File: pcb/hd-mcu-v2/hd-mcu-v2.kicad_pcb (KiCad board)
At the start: 2 copper layers, 70 x 48 mm, 27 parts

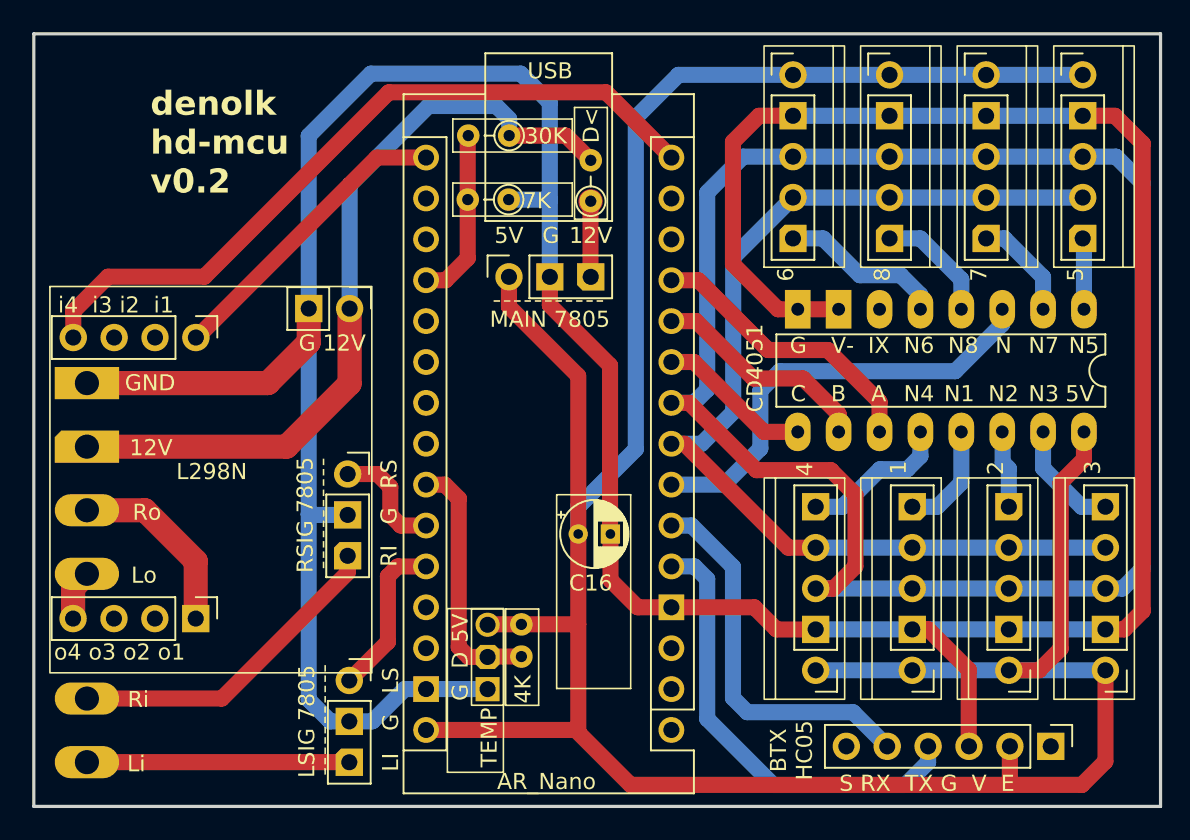
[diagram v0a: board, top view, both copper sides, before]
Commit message: refactor Ax sensor pin layout
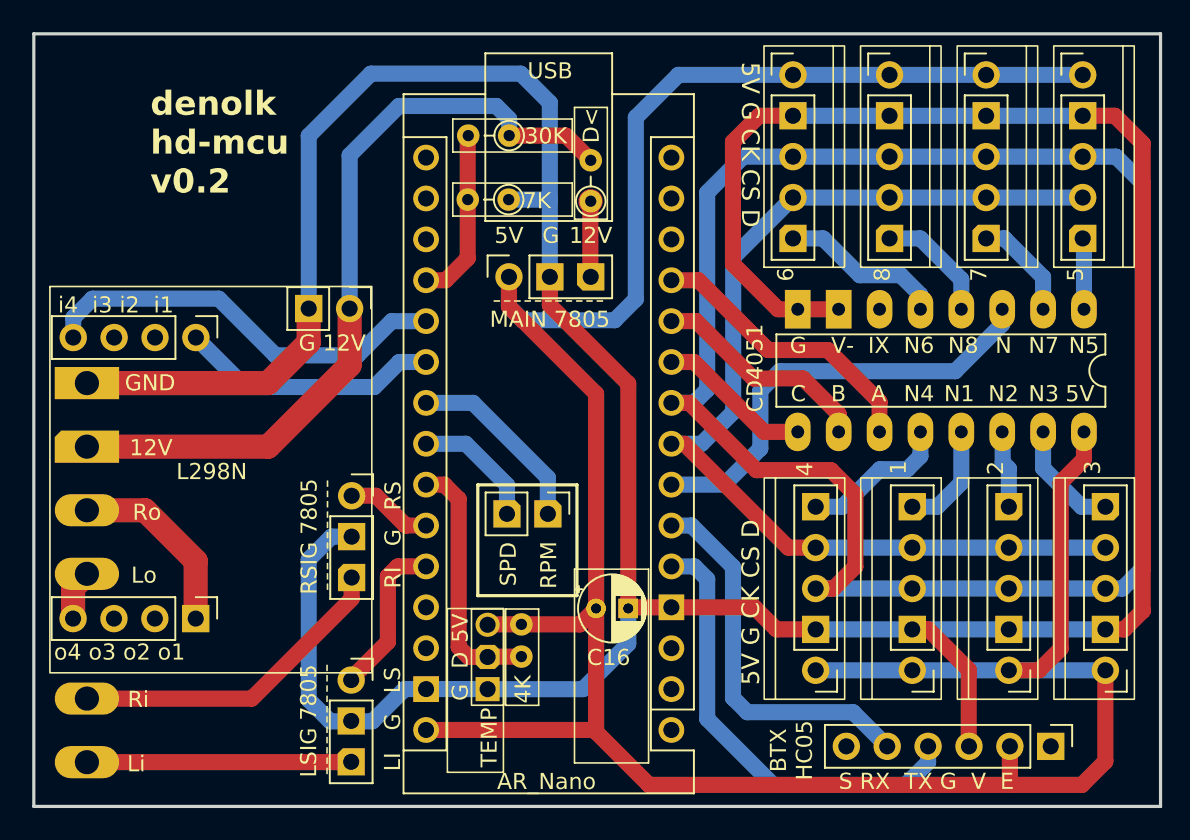
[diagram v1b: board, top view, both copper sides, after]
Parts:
- added REF**: C16, Capacitor_THT:CP_Radial_D4.0mm_P2.00mm, F.Cu at (59.6, 71.3)
- added REF**: PinHeader_1x02_P2.54mm_Vertical, Connector_PinHeader_2.54mm:PinHeader_1x02_P2.54mm_Vertical, F.Cu at (56.6, 65.5)
- REF**: moved to B.Cu
- moved REF** 4.76 mm to (59.6, 71.3)
- moved RSIG 7805 1.37 mm to (44.4, 64.3)
- moved LSIG 7805 0.12 mm to (44.3, 75.8)
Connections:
- REF** pad A1: D15 -> D_SIG_L_OUT
- REF** pad A2: D16 -> D_SIG_R_OUT
- REF** pad A3: D17 -> D_RPM
- REF** pad A4: D18 -> D_SPD
- REF** pad D12: D_SIG_L_OUT -> D12
- REF** pad D13: D_SIG_R_OUT -> D13
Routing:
- net D_SIG_L_OUT: track 46.1 -> 26.0 mm
- net D_RPM: track 0.00 -> 11.7 mm
- net D_SPD: track 0.00 -> 7.88 mm
- net 5V: track 180.1 -> 176.6 mm
- net D_SIG_R_OUT: track 18.9 -> 16.2 mm
- net GND: track 233.7 -> 231.5 mm
- net D_SIG_R_IN: track 7.26 -> 5.42 mm
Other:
- board text added: "5V G CK CS D"
- board text added: "RPM"
- board text added: "S RX TX G V E"
- board text added: "SPD"

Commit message: pcb routing optimize
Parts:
- moved 30K 12.6 mm to (44.2, 49.8), turned to 90 degrees
- moved REF** 11.0 mm to (59.4, 60.3) (x2)
- moved 7K 10.6 mm to (44.2, 42.1), turned to -90 degrees
- moved -> 5.54 mm to (56.6, 41.1), turned to 0 degrees
- moved MAIN 7805 5.09 mm to (54.1, 45.7)
- moved REF** 2.97 mm to (56.0, 62.6)
- renumbered D< to ->
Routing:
- net GND: track 231.5 -> 221.7 mm
- net 12V: track 54.4 -> 49.3 mm
- net D_SPD: track 7.88 -> 5.04 mm
- net D_RPM: track 11.7 -> 9.49 mm
- net D_VOLT: track 10.8 -> 10.2 mm

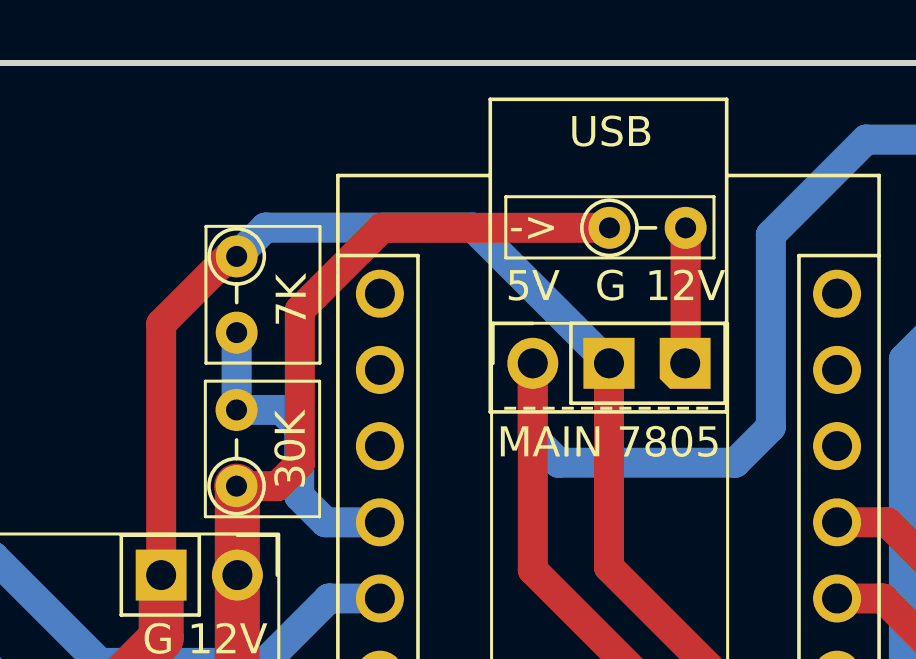
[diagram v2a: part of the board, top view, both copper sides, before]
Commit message: add serial commands
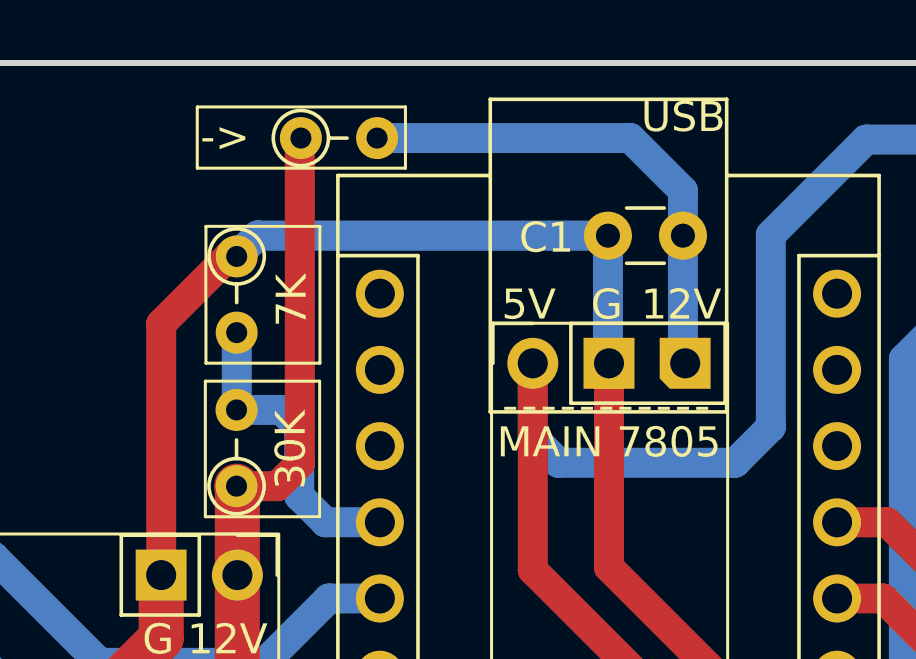
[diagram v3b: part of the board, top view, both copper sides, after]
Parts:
- added REF**: C1, Capacitor_THT:C_Disc_D3.0mm_W1.6mm_P2.50mm, F.Cu at (56.6, 41.4)
- moved -> 10.7 mm to (46.4, 38.1)
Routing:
- net 12V: track 49.3 -> 55.9 mm
- net GND: track 221.7 -> 223.9 mm
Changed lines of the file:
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@@
         (effects (font (size 1 1) (thickness 0.15)))
     )
-    (fp_text user "G" (at 2.570051 2.6 unlocked) (layer "F.SilkS")
-        (effects (font (size 1 1) (thickness 0.15)))
-    )
-    (fp_text user "5V" (at 2.570051 0 unlocked) (layer "F.SilkS")
-        (effects (font (size 1 1) (thickness 0.15)))
-    )
-    (fp_text user "12V" (at 2.570051 5.08 unlocked) (layer "F.SilkS")
+    (fp_text user "G" (at 1.955 2.465 unlocked) (layer "F.SilkS")
+        (effects (font (size 1 1) (thickness 0.15)))
+    )
+    (fp_text user "5V" (at 1.955 -0.135 unlocked) (layer "F.SilkS")
+        (effects (font (size 1 1) (thickness 0.15)))
+    )
+    (fp_text user "12V" (at 1.955 4.945 unlocked) (layer "F.SilkS")
         (effects (font (size 1 1) (thickness 0.15)))
     )
@@
         (effects (font (size 1 1) (thickness 0.15)))
     )
-    (fp_text user "USB" (at 7.5375 40.945 unlocked) (layer "F.SilkS")
+    (fp_text user "USB" (at 5.1275 41.445 unlocked) (layer "F.SilkS")
         (effects (font (size 1 1) (thickness 0.15)))
     )
@@
   )
   (footprint "Resistor_THT:R_Axial_DIN0204_L3.6mm_D1.6mm_P2.54mm_Vertical" (layer "F.Cu")
-    (at 56.65 41.14)
+    (at 46.365 38.1475)
     (descr "Resistor, Axial_DIN0204 series, Axial, Vertical, pin pitch=2.54mm, 0.167W, length*diameter=3.6*1.6mm^2, http://cdn-reichelt.de/documents/datenblatt/B400/1_4W%23YAG.pdf")
     (tags "Resistor Axial_DIN0204 series Axial Vertical pin pitch 2.54mm 0.167W length 3.6mm diameter 1.6mm")
@@
     (pad "3" thru_hole oval (at 0 0 180) (size 4 2) (drill 1.5) (layers "*.Cu" "*.Mask")
       (net 6 "SIG_R_OUT"))
+  )
+  (footprint "Capacitor_THT:C_Disc_D3.0mm_W1.6mm_P2.50mm" (layer "F.Cu")
+    (at 56.6 41.4)
+    (descr "C, Disc series, Radial, pin pitch=2.50mm, , diameter*width=3.0*1.6mm^2, Capacitor, http://www.vishay.com/docs/45233/krseries.pdf")
+    (tags "C Disc series Radial pin pitch 2.50mm  diameter 3.0mm width 1.6mm Capacitor")
+    (attr through_hole)
+    (fp_text reference "REF**" (at 1.25 -2.05) (layer "F.SilkS") hide
+        (effects (font (size 1 1) (thickness 0.15)))
+    )
+    (fp_text value "C1" (at -2.05 0.07) (layer "F.SilkS")
+        (effects (font (size 1 1) (thickness 0.15)))
+    )
+    (fp_text user "${REFERENCE}" (at 1.25 0) (layer "F.Fab") hide
+        (effects (font (size 0.6 0.6) (thickness 0.09)))
+    )
+    (fp_line (start 0.621 -0.92) (end 1.879 -0.92)
+      (stroke (width 0.12) (type solid)) (layer "F.SilkS"))
+    (fp_line (start 0.621 0.92) (end 1.879 0.92)
+      (stroke (width 0.12) (type solid)) (layer "F.SilkS"))
+    (fp_line (start -1.05 -1.05) (end -1.05 1.05)
+      (stroke (width 0.05) (type solid)) (layer "F.CrtYd"))
+    (fp_line (start -1.05 1.05) (end 3.55 1.05)
+      (stroke (width 0.05) (type solid)) (layer "F.CrtYd"))
+    (fp_line (start 3.55 -1.05) (end -1.05 -1.05)
+      (stroke (width 0.05) (type solid)) (layer "F.CrtYd"))
+    (fp_line (start 3.55 1.05) (end 3.55 -1.05)
+      (stroke (width 0.05) (type solid)) (layer "F.CrtYd"))
+    (fp_line (start -0.25 -0.8) (end -0.25 0.8)
+      (stroke (width 0.1) (type solid)) (layer "F.Fab"))
+    (fp_line (start -0.25 0.8) (end 2.75 0.8)
+      (stroke (width 0.1) (type solid)) (layer "F.Fab"))
+    (fp_line (start 2.75 -0.8) (end -0.25 -0.8)
+      (stroke (width 0.1) (type solid)) (layer "F.Fab"))
+    (fp_line (start 2.75 0.8) (end 2.75 -0.8)
+      (stroke (width 0.1) (type solid)) (layer "F.Fab"))
+    (pad "1" thru_hole circle (at 0 0) (size 1.6 1.6) (drill 0.8) (layers "*.Cu" "*.Mask")
+      (net 1 "GND"))
+    (pad "2" thru_hole circle (at 2.5 0) (size 1.6 1.6) (drill 0.8) (layers "*.Cu" "*.Mask")
+      (net 2 "12V"))
+    (model "${KICAD6_3DMODEL_DIR}/Capacitor_THT.3dshapes/C_Disc_D3.0mm_W1.6mm_P2.50mm.wrl"
+      (offset (xyz 0 0 0))
+      (scale (xyz 1 1 1))
+      (rotate (xyz 0 0 0))
+    )
   )
   (footprint "Connector_PinHeader_2.54mm:Socker_PinHeader_1x05_P2.54mm_Dualside" (layer "F.Cu")
@@
   (gr_rect (start 58.099604 57.9) (end 62.699604 69.94)
     (stroke (width 0.1) (type default)) (fill none) (layer "B.SilkS"))
-  (gr_rect (start 60.135 40.1025) (end 53.195 42.1425)
+  (gr_rect (start 49.85 37.11) (end 42.91 39.15)
     (stroke (width 0.1) (type default)) (fill none) (layer "F.SilkS"))
   (gr_rect (start 50.3225 71.355) (end 53.8025 81.525)
@@
   (segment (start 69.395 71.275) (end 64.2375 71.275) (width 1) (layer "F.Cu") (net 1))
   (segment (start 41.7075 54.815) (end 41.7075 52.715) (width 1.5) (layer "F.Cu") (net 1))
+  (segment (start 44.9375 41.4) (end 56.6 41.4) (width 1) (layer "B.Cu") (net 1))
   (segment (start 44.375 66.885) (end 43.125 66.885) (width 1) (layer "B.Cu") (net 1))
   (segment (start 43.0425 78.36) (end 45.6625 78.36) (width 1) (layer "B.Cu") (net 1))
   (segment (start 57.99 76.36) (end 63.075 71.275) (width 1) (layer "B.Cu") (net 1))
   (segment (start 63.075 71.275) (end 64.2375 71.275) (width 1) (layer "B.Cu") (net 1))
-  (segment (start 56.635 45.655) (end 52.11 41.13) (width 1) (layer "B.Cu") (net 1))
   (segment (start 41.7075 77.025) (end 43.0425 78.36) (width 1) (layer "B.Cu") (net 1))
   (segment (start 41.7075 68.3025) (end 41.7075 77.025) (width 1) (layer "B.Cu") (net 1))
   (segment (start 45.6625 78.36) (end 47.6675 76.355) (width 1) (layer "B.Cu") (net 1))
-  (segment (start 52.11 41.13) (end 45.1875 41.13) (width 1) (layer "B.Cu") (net 1))
   (segment (start 52.82 76.36) (end 57.99 76.36) (width 1) (layer "B.Cu") (net 1))
   (segment (start 47.6675 76.355) (end 48.9975 76.355) (width 1) (layer "B.Cu") (net 1))
   (segment (start 73.2025 72.6475) (end 91.2025 72.6475) (width 1) (layer "B.Cu") (net 1))
-  (segment (start 45.1875 41.13) (end 44.225 42.0925) (width 1) (layer "B.Cu") (net 1))
   (segment (start 43.125 66.885) (end 41.7075 68.3025) (width 1) (layer "B.Cu") (net 1))
+  (segment (start 44.9275 41.39) (end 44.9375 41.4) (width 1) (layer "B.Cu") (net 1))
   (segment (start 52.815 76.355) (end 52.82 76.36) (width 1) (layer "B.Cu") (net 1))
   (segment (start 48.9975 76.355) (end 52.815 76.355) (width 1) (layer "B.Cu") (net 1))
+  (segment (start 56.6 41.4) (end 56.6 45.62) (width 1) (layer "B.Cu") (net 1))
+  (segment (start 44.9275 41.39) (end 44.225 42.0925) (width 1) (layer "B.Cu") (net 1))
   (segment (start 89.7925 40.7375) (end 71.7925 40.7375) (width 1) (layer "B.Cu") (net 1))
+  (segment (start 56.6 45.62) (end 56.635 45.655) (width 1) (layer "B.Cu") (net 1))
   (segment (start 44.2475 57.7325) (end 44.2475 52.715) (width 1.5) (layer "F.Cu") (net 2))
-  (segment (start 46.33 49) (end 46.33 43.881179) (width 1) (layer "F.Cu") (net 2))
+  (segment (start 44.22 49.75) (end 45.58 49.75) (width 1) (layer "F.Cu") (net 2))
   (segment (start 59.19 45.64) (end 59.175 45.655) (width 1) (layer "F.Cu") (net 2))
-  (segment (start 59.19 41.14) (end 59.19 45.64) (width 1) (layer "F.Cu") (net 2))
   (segment (start 44.2475 52.715) (end 44.2475 49.7775) (width 1.5) (layer "F.Cu") (net 2))
-  (segment (start 49.071179 41.14) (end 56.65 41.14) (width 1) (layer "F.Cu") (net 2))
-  (segment (start 44.22 49.75) (end 45.58 49.75) (width 1) (layer "F.Cu") (net 2))
+  (segment (start 46.33 38.1825) (end 46.365 38.1475) (width 1) (layer "F.Cu") (net 2))
+  (segment (start 59.1 45.58) (end 59.175 45.655) (width 1) (layer "F.Cu") (net 2))
   (segment (start 27.9275 61.295) (end 40.685 61.295) (width 1.5) (layer "F.Cu") (net 2))
   (segment (start 44.2475 49.7775) (end 44.22 49.75) (width 1.5) (layer "F.Cu") (net 2))
-  (segment (start 46.33 43.881179) (end 49.071179 41.14) (width 1) (layer "F.Cu") (net 2))
+  (segment (start 46.33 49) (end 46.33 38.1825) (width 1) (layer "F.Cu") (net 2))
+  (segment (start 40.685 61.295) (end 44.2475 57.7325) (width 1.5) (layer "F.Cu") (net 2))
   (segment (start 45.58 49.75) (end 46.33 49) (width 1) (layer "F.Cu") (net 2))
-  (segment (start 40.685 61.295) (end 44.2475 57.7325) (width 1.5) (layer "F.Cu") (net 2))
+  (segment (start 48.905 38.1475) (end 57.3475 38.1475) (width 1) (layer "B.Cu") (net 2))
+  (segment (start 59.1 45.58) (end 59.175 45.655) (width 1) (layer "B.Cu") (net 2))
+  (segment (start 59.1 39.9) (end 59.1 41.4) (width 1) (layer "B.Cu") (net 2))
+  (segment (start 59.1 41.4) (end 59.1 45.58) (width 1) (layer "B.Cu") (net 2))
+  (segment (start 57.3475 38.1475) (end 59.1 39.9) (width 1) (layer "B.Cu") (net 2))
   (segment (start 44.2225 80.895) (end 44.2275 80.9) (width 1) (layer "F.Cu") (net 3))
   (segment (start 27.9275 80.895) (end 44.2225 80.895) (width 1) (layer "F.Cu") (net 3))
